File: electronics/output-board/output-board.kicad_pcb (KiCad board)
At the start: 4 copper layers, 105.2 x 77.5 mm, 101 parts, among them J1 Conn_01x02_Male, J10 Conn_01x02_Male, J11 Conn_01x02_Male, J12 Conn_01x02_Male, J13 Conn_01x02_Male, J14 Arming switch, J15 Conn_01x02_Male, J16 Conn_01x02_Male, J17 Conn_01x02_Male, J18 Conn_01x02_Male, J19 Extra IO, J2 Conn_01x02_Male, J20 Ignition Detector, J3 12V In, J4 Conn_01x02, J5 SWD Header, J6 Conn_01x02, J7 Conn_01x02_Male, J8 Conn_01x02_Male, J9 Conn_01x02_Male, SW1 SW_Push_Dual, U1 MAX33012EASA+, U2 LD3985M33R_SOT23, U3 STM32F105VBH6, Y1 25MHz 9pF

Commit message: Started updating the output board
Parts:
- Y1: value 25MHz 9pF -> 36MHz 9pF
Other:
- board text added: "5V"
- board text added: "CLK"
- board text added: "DIO"
- board text added: "GND"
- board text removed: "DEBUG"
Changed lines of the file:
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@@
       (effects (font (size 1 1) (thickness 0.15)))
     )
-    (fp_text value "25MHz 9pF" (at 0 3.048) (layer "F.SilkS")
+    (fp_text value "36MHz 9pF" (at 0 3.048) (layer "F.SilkS")
       (effects (font (size 1 1) (thickness 0.15)))
     )
@@
     (fp_line (start 1.6 1.25) (end 1.6 -1.25) (layer "F.Fab") (width 0.1))
     (fp_line (start 1.6 -1.25) (end -1.6 -1.25) (layer "F.Fab") (width 0.1))
-    (pad "1" smd rect locked (at -1.1 0.85 180) (size 1.4 1.2) (layers "F.Cu" "F.Paste" "F.Mask")
+    (pad "1" smd rect (at -1.125 0.775 180) (size 1.3 1) (layers "F.Cu" "F.Paste" "F.Mask")
       (net 45 "Net-(C10-Pad2)") (pinfunction "1") (pintype "passive"))
-    (pad "2" smd rect locked (at 1.1 0.85 180) (size 1.4 1.2) (layers "F.Cu" "F.Paste" "F.Mask")
+    (pad "2" smd rect (at 1.125 0.775 180) (size 1.3 1) (layers "F.Cu" "F.Paste" "F.Mask")
       (net 6 "GND") (pinfunction "2") (pintype "passive"))
-    (pad "3" smd rect locked (at 1.1 -0.85 180) (size 1.4 1.2) (layers "F.Cu" "F.Paste" "F.Mask")
+    (pad "3" smd rect (at 1.125 -0.775 180) (size 1.3 1) (layers "F.Cu" "F.Paste" "F.Mask")
       (net 46 "Net-(C11-Pad2)") (pinfunction "3") (pintype "passive"))
-    (pad "4" smd rect locked (at -1.1 -0.85 180) (size 1.4 1.2) (layers "F.Cu" "F.Paste" "F.Mask")
+    (pad "4" smd rect (at -1.125 -0.775 180) (size 1.3 1) (layers "F.Cu" "F.Paste" "F.Mask")
       (net 6 "GND") (pinfunction "4") (pintype "passive"))
     (model "${KICAD6_3DMODEL_DIR}/Crystal.3dshapes/Crystal_SMD_3225-4Pin_3.2x2.5mm.wrl"
@@
     (effects (font (size 1.2 1.5) (thickness 0.3)))
   )
+  (gr_text "GND" (at 36.322 49.784) (layer "F.SilkS")
+    (effects (font (size 1 1) (thickness 0.15)))
+  )
+  (gr_text "CLK" (at 36.322 44.704) (layer "F.SilkS")
+    (effects (font (size 1 1) (thickness 0.15)))
+  )
   (gr_text "8" (at 53.848 104.394) (layer "F.SilkS")
     (effects (font (size 1.2 1.5) (thickness 0.3)))
@@
     (effects (font (size 1.2 1.5) (thickness 0.3)))
   )
+  (gr_text "5V" (at 36.322 47.244) (layer "F.SilkS")
+    (effects (font (size 1 1) (thickness 0.15)))
+  )
   (gr_text "CAN" (at 30.099 51.0032) (layer "F.SilkS")
     (effects (font (size 1.2 1.5) (thickness 0.3)))
@@
     (effects (font (size 1.2 1.5) (thickness 0.3)))
   )
-  (gr_text "DEBUG" (at 36.3474 45.8216 270) (layer "F.SilkS")
-    (effects (font (size 1.2 1.5) (thickness 0.3)))
-  )
   (gr_text "RESET" (at 128.397 66.294 270) (layer "F.SilkS")
     (effects (font (size 1.2 1.5) (thickness 0.3)))
@@
     (effects (font (size 1.2 1.5) (thickness 0.3)))
   )
+  (gr_text "DIO" (at 36.322 42.164) (layer "F.SilkS")
+    (effects (font (size 1 1) (thickness 0.15)))
+  )
   (gr_text "9" (at 66.548 104.394) (layer "F.SilkS")

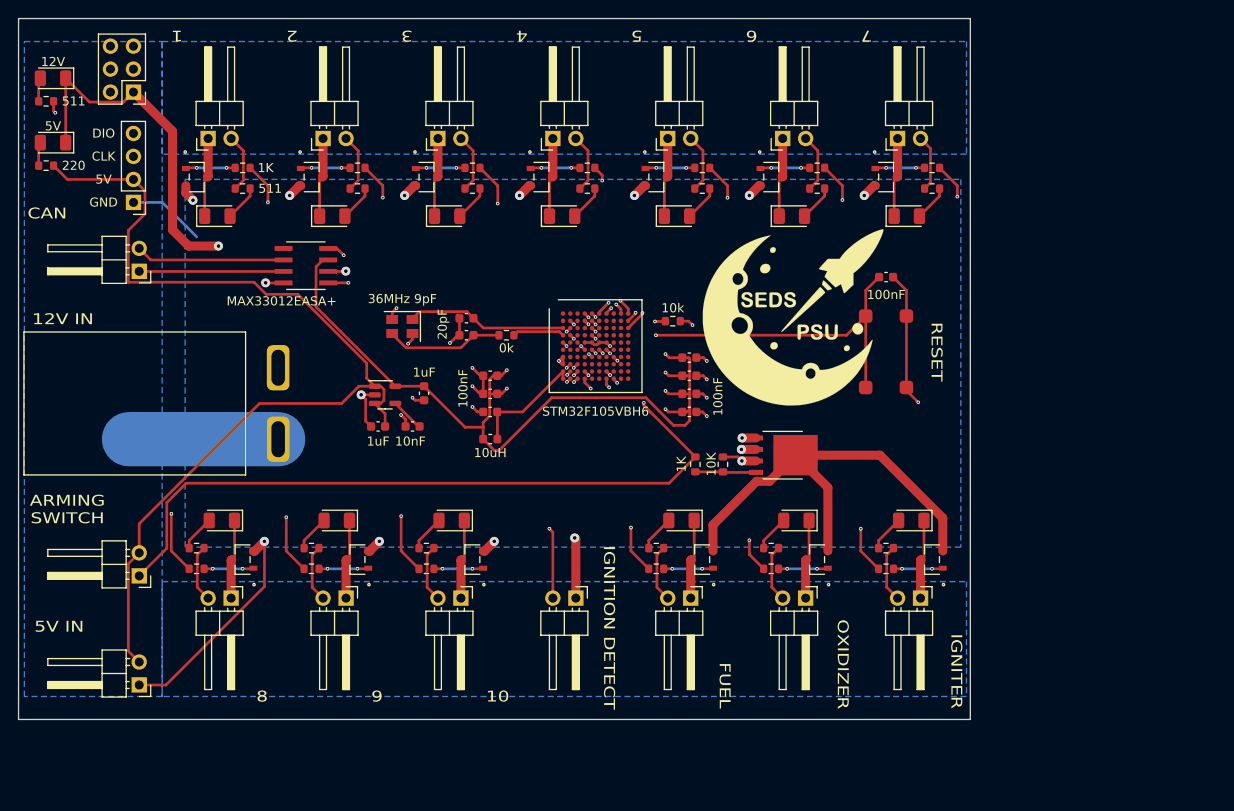
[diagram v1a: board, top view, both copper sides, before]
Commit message: Revising Output Board
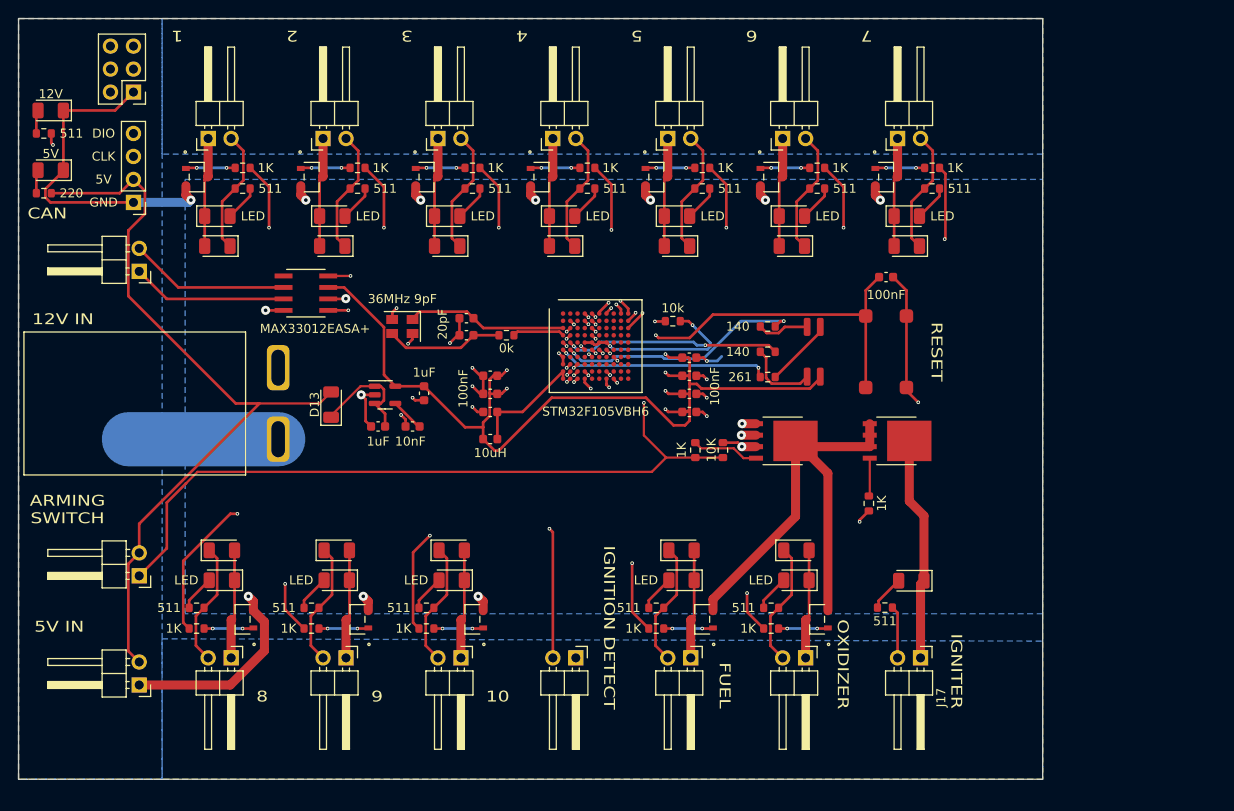
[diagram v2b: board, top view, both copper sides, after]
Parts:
- removed Ref**: Val**, CustomFootprints:seds-logo
- added D16: LED, LED_SMD:LED_1206_3216Metric, F.Cu at (125.6, 91.6)
- added D17: 1N4007, Diode_SMD:D_1206_3216Metric, F.Cu at (49.4, 88.2)
- added D18: 1N4007, Diode_SMD:D_1206_3216Metric, F.Cu at (48.9, 54.6)
- added D19: 1N4007, Diode_SMD:D_1206_3216Metric, F.Cu at (61.6, 54.6)
- added D20: 1N4007, Diode_SMD:D_1206_3216Metric, F.Cu at (74.3, 54.6)
- added D21: 1N4007, Diode_SMD:D_1206_3216Metric, F.Cu at (87.0, 54.6)
- added D22: 1N4007, Diode_SMD:D_1206_3216Metric, F.Cu at (99.7, 54.6)
- added D23: 1N4007, Diode_SMD:D_1206_3216Metric, F.Cu at (112.4, 54.6)
- added D24: 1N4007, Diode_SMD:D_1206_3216Metric, F.Cu at (125.1, 54.6)
- added D25: 1N4007, Diode_SMD:D_1206_3216Metric, F.Cu at (74.8, 88.2)
- added D26: 1N4007, Diode_SMD:D_1206_3216Metric, F.Cu at (62.1, 88.2)
- added D27: 1N4007, Diode_SMD:D_1206_3216Metric, F.Cu at (100.2, 88.2)
- added D28: 1N4007, Diode_SMD:D_1206_3216Metric, F.Cu at (112.9, 88.2)
- added D29: LED_RGBA, CustomFootprints:RGB LED, F.Cu at (114.8, 66.3)
- added R33: 261, Resistor_SMD:R_0603_1608Metric, F.Cu at (109.7, 69.1)
- added R34: 140, Resistor_SMD:R_0603_1608Metric, F.Cu at (109.7, 63.5)
- added R35: 140, Resistor_SMD:R_0603_1608Metric, F.Cu at (109.7, 66.3)
- D13: value LED -> 1N4007; footprint LED_SMD:LED_1206_3216Metric -> Diode_SMD:D_1206_3216Metric
- MOSFET13: value BSS806NEH6327XTSA1 -> BUK9Y21-40E; footprint MOSFET:BSS806NEH6327XTSA1 -> MOSFET 2:BUK9Y21-40E
- moved D13 40.8 mm to (61.5, 72.1), turned to 90 degrees
- moved D11 26.2 mm to (100.2, 91.5)
- moved J15 26.2 mm to (101.2, 100.1)
- moved J17 26.2 mm to (126.6, 100.1)
- moved MOSFET11 26.2 mm to (102.5, 95.9)
- moved R25 26.2 mm to (97.4, 96.9)
- moved R26 26.2 mm to (97.4, 94.6)
- moved R30 26.1 mm to (122.7, 94.6)
- moved MOSFET13 25.2 mm to (124.0, 76.1), turned to -90 degrees
- moved R29 24.6 mm to (120.9, 83.1), turned to 90 degrees
- moved D10 6.60 mm to (62.1, 91.5)
- moved D12 6.60 mm to (112.9, 91.5)
- moved D2 6.60 mm to (49.4, 91.5)
- moved D9 6.60 mm to (74.8, 91.5)
- moved J12 6.60 mm to (75.8, 100.1)
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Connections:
- net /Ignition MOSFET/INPUT renamed Net-(R29-Pad1)
- C1 pad 1: +5V -> Net-(C1-Pad1)
- D13 pad 1: Net-(D13-Pad1) -> Net-(C1-Pad1)
- D13 pad 2: Net-(D13-Pad2) -> +5V
- J17 pad 1: Net-(D13-Pad1) -> Net-(D16-Pad1)
- MOSFET10 pad 5: /Ignition MOSFET/GROUND -> /MOSFET-sheet10/GROUND
- MOSFET11 pad 2: /Ignition MOSFET/GROUND -> /MOSFET-sheet10/GROUND
- MOSFET12 pad 2: /Ignition MOSFET/GROUND -> /MOSFET-sheet10/GROUND
- MOSFET13 pad 1: Net-(MOSFET13-Pad1) -> /MOSFET-sheet10/GROUND
- MOSFET13 pad 2: /Ignition MOSFET/GROUND -> /MOSFET-sheet10/GROUND
- MOSFET13 pad 3: Net-(D13-Pad1) -> /MOSFET-sheet10/GROUND
- R12 pad 1: Net-(MOSFET10-Pad4) -> Net-(J14-Pad1)
- R12 pad 2: Net-(J14-Pad1) -> Net-(MOSFET10-Pad4)
- R13 pad 1: Net-(MOSFET10-Pad4) -> Net-(J14-Pad1)
- R29 pad 2: Net-(MOSFET13-Pad1) -> Net-(MOSFET13-Pad4)
- R30 pad 2: Net-(D13-Pad2) -> Net-(D16-Pad2)
- U2 pad 1: +5V -> Net-(C1-Pad1)
- U2 pad 3: +5V -> Net-(C1-Pad1)
- U3 pad E2: unconnected-(U3-PadE2) -> Net-(R35-Pad1)
- U3 pad F1: unconnected-(U3-PadF1) -> Net-(R33-Pad1)
- U3 pad F2: unconnected-(U3-PadF2) -> Net-(R34-Pad1)
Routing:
- net +12V: track 100.9 -> 189.0 mm
- net /MOSFET-sheet10/GROUND: track 0.00 -> 53.8 mm
- net /Ignition MOSFET/GROUND: track 50.1 -> 0.00 mm
- net Net-(R34-Pad1): track 0.00 -> 27.3 mm, vias 0 -> 2
- net Net-(D16-Pad1): track 0.00 -> 24.8 mm
- net Net-(R35-Pad1): track 0.00 -> 23.8 mm, vias 0 -> 2
- net Net-(R33-Pad1): track 0.00 -> 23.5 mm, vias 0 -> 2
- net +5V: track 110.2 -> 86.9 mm
- net Net-(R29-Pad1): track 22.6 -> 36.0 mm
- net Net-(C1-Pad1): track 0.00 -> 12.9 mm
- net +3V3: track 146.2 -> 157.2 mm
- net /MOSFET-sheet10/INPUT: track 40.6 -> 30.3 mm
- net Net-(D13-Pad1): track 8.74 -> 0.00 mm
- net Net-(D29-Pad3): track 0.00 -> 8.28 mm
- net Net-(D29-Pad1): track 0.00 -> 7.61 mm
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- added copper zone on F.Cu, net GND
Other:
- board size 105.2 x 77.5 mm -> 113.2 x 84.1 mm

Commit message: More output board revisions
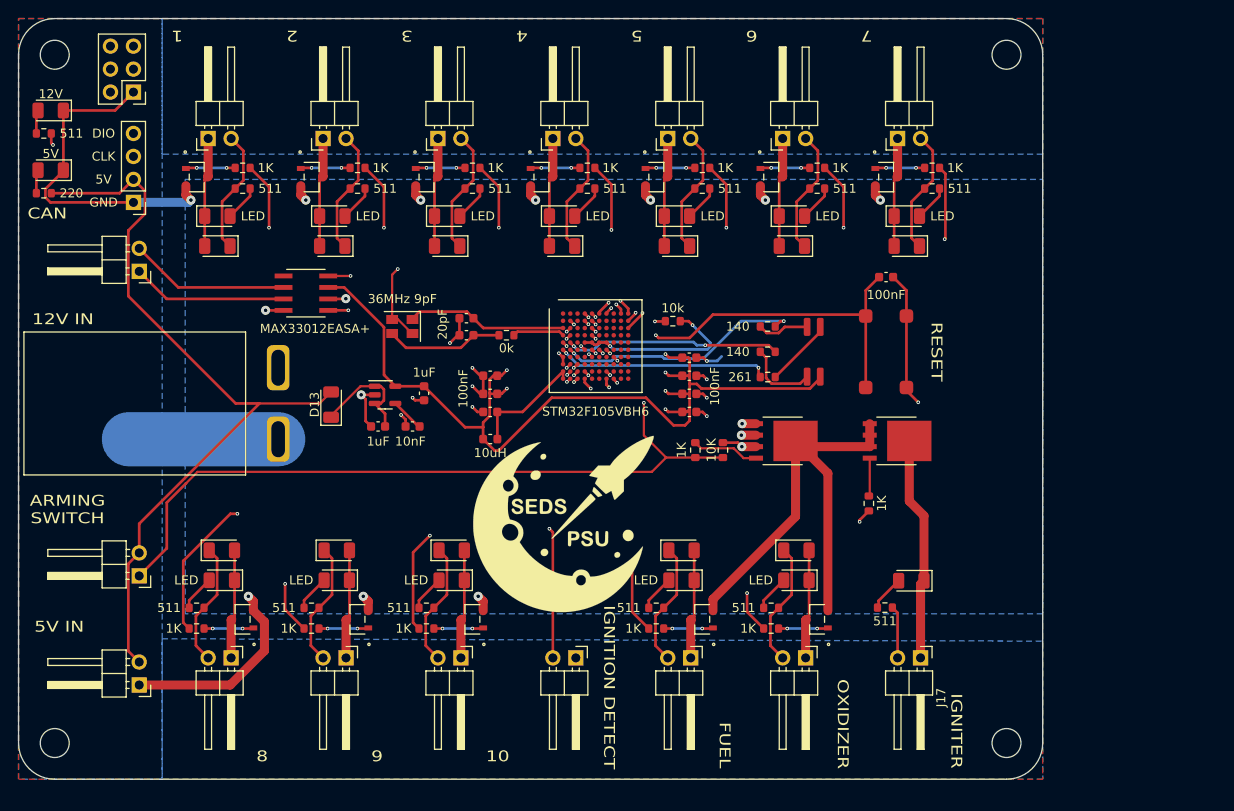
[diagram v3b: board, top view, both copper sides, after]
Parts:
- added HOLE1: MountingHole_3.2mm_M3, MountingHole:MountingHole_3.2mm_M3, F.Cu at (30.9, 33.5)
- added HOLE1: MountingHole_3.2mm_M3, MountingHole:MountingHole_3.2mm_M3, F.Cu at (136.1, 109.5)
- added HOLE1: MountingHole_3.2mm_M3, MountingHole:MountingHole_3.2mm_M3, F.Cu at (136.1, 33.5)
- added HOLE1: MountingHole_3.2mm_M3, MountingHole:MountingHole_3.2mm_M3, F.Cu at (30.9, 109.5)
- added Ref**: Val**, CustomFootprints:seds-logo, F.Cu at (87.1, 85.1)
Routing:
- net GND: track 149.2 -> 155.3 mm, vias 33 -> 32
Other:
- outline, holes or cut-outs redrawn

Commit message: Finishing touches on output board rev 2
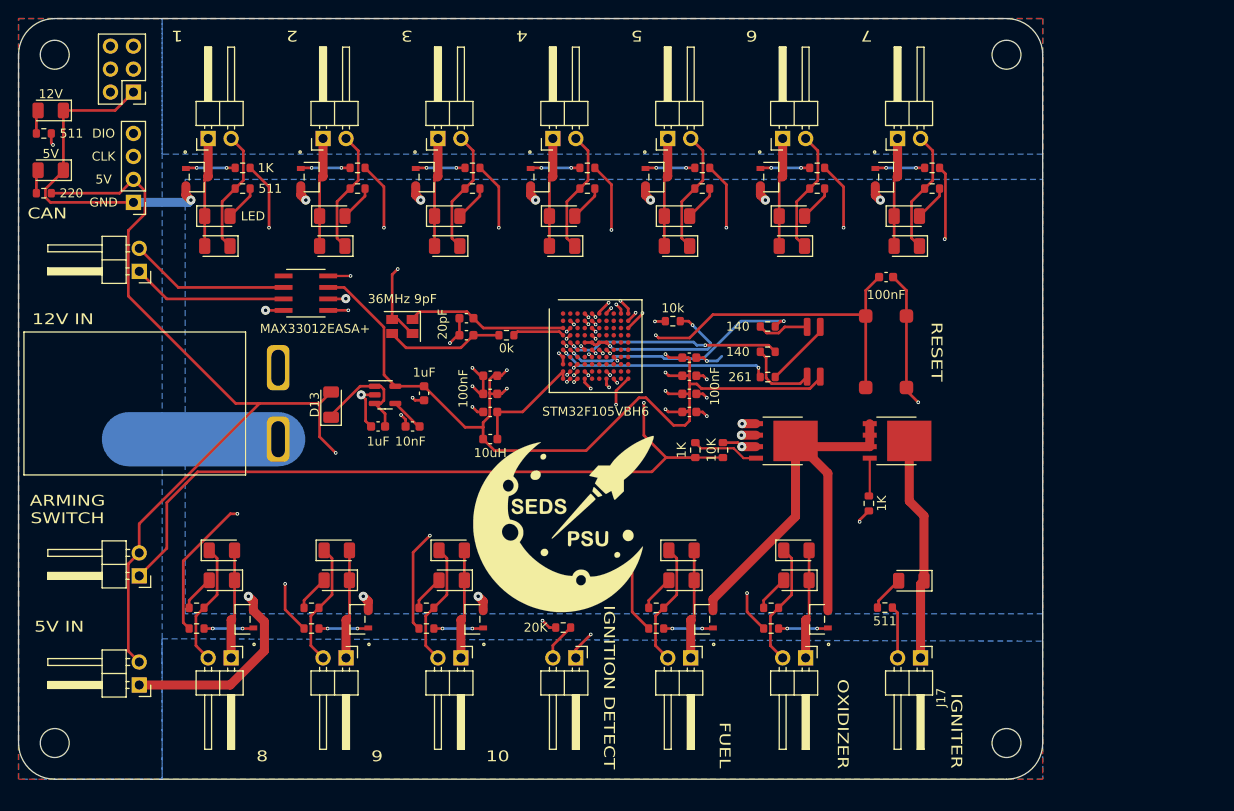
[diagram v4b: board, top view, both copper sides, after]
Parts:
- added R36: 20K, Resistor_SMD:R_0603_1608Metric, F.Cu at (87.1, 96.8)
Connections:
- J20 pad 1: GND -> Net-(U3-PadK10)
- U3 pad H2: Net-(J20-Pad2) -> unconnected-(U3-PadH2)
- U3 pad K10: unconnected-(U3-PadK10) -> Net-(U3-PadK10)
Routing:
- net +5V: track 86.9 -> 125.4 mm, vias 0 -> 2
- net Net-(U3-PadK10): track 0.00 -> 33.3 mm, vias 0 -> 2
- net Net-(J20-Pad2): track 33.6 -> 4.17 mm, vias 2 -> 0

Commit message: changed can transciever
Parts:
- added C14: 100nF, Capacitor_SMD:C_0603_1608Metric, F.Cu at (157.5, 70.1)
- added R36: 120, Resistor_SMD:R_0603_1608Metric, F.Cu at (157.5, 72.6)
- added U1: MAX33014EATB+, MAX33014E:MAX33014EATB&plus_, F.Cu at (150.1, 77.1)
- renumbered R36 to R37

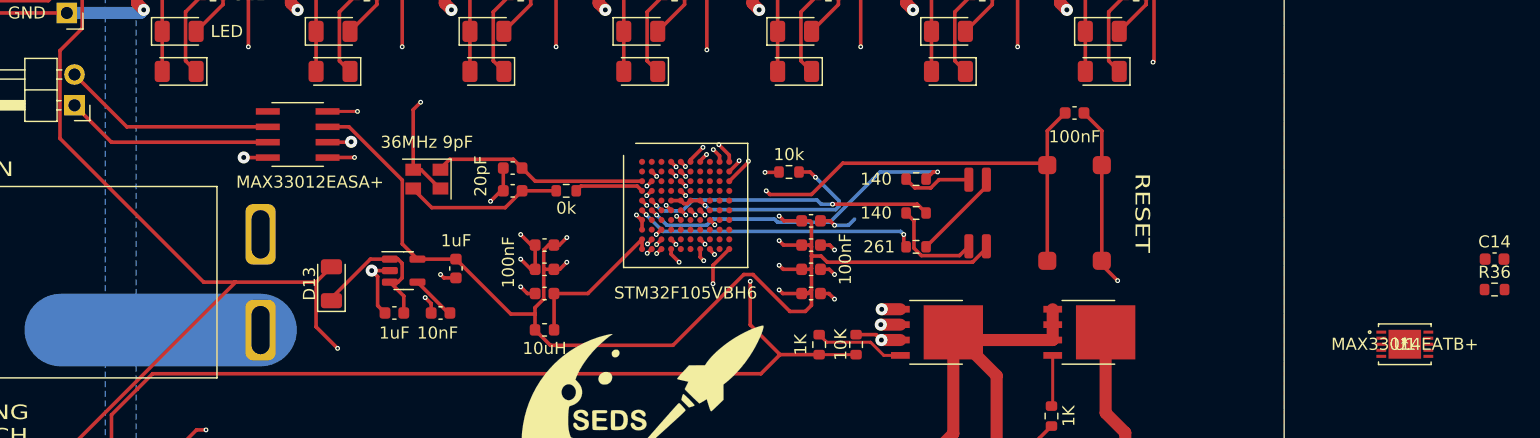
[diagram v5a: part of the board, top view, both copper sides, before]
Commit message: New transceiver on output board
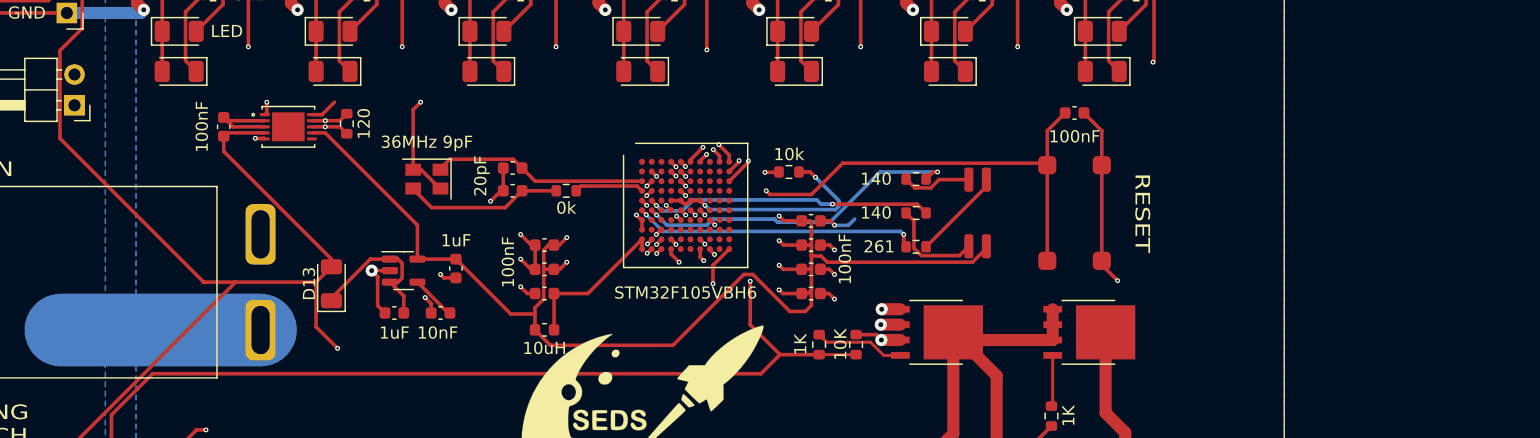
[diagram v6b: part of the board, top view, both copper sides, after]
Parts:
- removed the U1 at (58.7, 59.8)
- moved C14 105.5 mm to (52.6, 59.2), turned to 90 degrees
- moved R36 95.7 mm to (62.7, 58.9), turned to 90 degrees
- moved U1 93.9 mm to (57.9, 59.2)
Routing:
- net +5V: track 125.4 -> 143.4 mm
- net /CAN_RX: track 39.1 -> 49.4 mm
- net Net-(J6-Pad2): track 17.7 -> 26.7 mm, vias 0 -> 1
- net Net-(J6-Pad1): track 17.2 -> 25.0 mm, vias 0 -> 1
- net GND: track 155.3 -> 160.8 mm, vias 32 -> 30
- net /CAN_TX: track 38.0 -> 43.5 mm
